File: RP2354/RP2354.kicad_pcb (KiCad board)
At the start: 2 copper layers, 37.4 x 23.2 mm, 38 parts, among them J1 USB_C_Receptacle_USB2.0_14P, J2 SWD, J3 Conn_01x12_Pin, J4 Conn_01x12_Pin, U1 TCR8BM33A_L3F, U14 RP2354A, Y1 Crystal

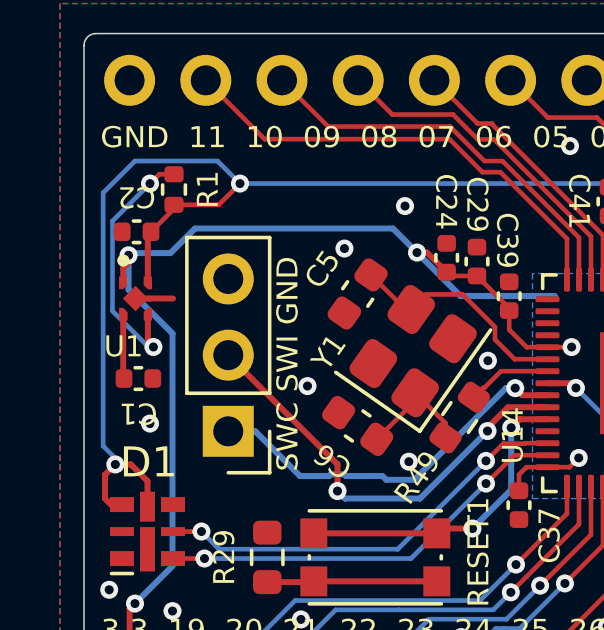
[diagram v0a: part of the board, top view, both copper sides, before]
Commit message: MPN's added for most parts. iBom export
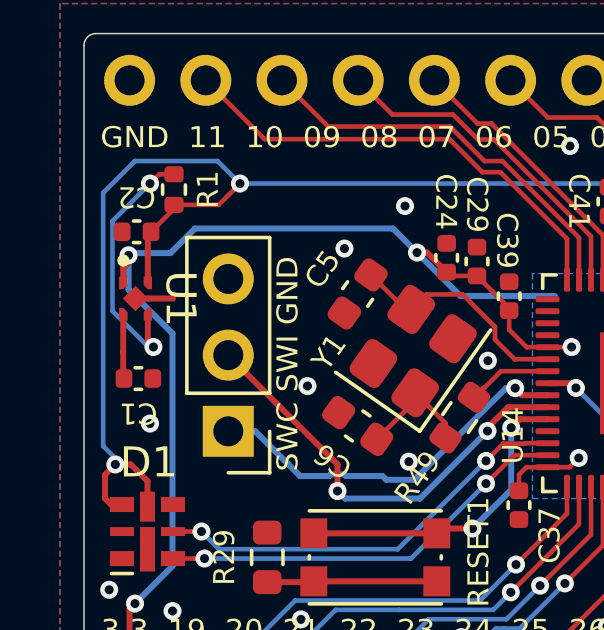
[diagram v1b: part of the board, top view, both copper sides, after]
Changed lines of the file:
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@@
 			)
 		)
+		(property "MFGR" "Adafruit (10-pack!)"
+			(at 0 0 0)
+			(unlocked yes)
+			(layer "F.Fab")
+			(hide yes)
+			(effects
+				(font
+					(size 1 1)
+					(thickness 0.15)
+				)
+			)
+		)
+		(property "MPN" "3341"
+			(at 0 0 0)
+			(unlocked yes)
+			(layer "F.Fab")
+			(hide yes)
+			(effects
+				(font
+					(size 1 1)
+					(thickness 0.15)
+				)
+			)
+		)
 		(property ki_fp_filters "LED*APA102*")
 		(sheetname "/")
@@
 		(tags "TCR8BM33A_L3F ")
 		(property "Reference" "U1"
-			(at 1.601769 0.399755 0)
+			(at 0 -1.5 270)
 			(unlocked yes)
 			(layer "F.SilkS")
 			(effects
 				(font
-					(size 0.7 0.7)
-					(thickness 0.1)
+					(size 1 1)
+					(thickness 0.15)
 				)
 			)
@@
 			)
 		)
+		(property "MFGR" "Toshiba Semiconductor and Storage"
+			(at 0 0 270)
+			(unlocked yes)
+			(layer "F.Fab")
+			(hide yes)
+			(effects
+				(font
+					(size 1 1)
+					(thickness 0.15)
+				)
+			)
+		)
+		(property "MPN" "TCR8BM33A,L3F"
+			(at 0 0 270)
+			(unlocked yes)
+			(layer "F.Fab")
+			(hide yes)
+			(effects
+				(font
+					(size 1 1)
+					(thickness 0.15)
+				)
+			)
+		)
 		(property ki_fp_filters "DFN5B_TOS")
 		(sheetname "/")
@@
 			(net 4 "+3V3")
 			(pinfunction "VOUT")
-			(pintype "output")
+			(pintype "power_out")
 		)
 		(pad "2" smd roundrect
@@
 			(net 58 "/VBIAS")
 			(pinfunction "VBIAS")
-			(pintype "power_in")
+			(pintype "input")
 		)
 		(pad "3" smd roundrect
@@
 			)
 		)
-		(property "MFGR" ""
+		(property "MFGR" "Samsung"
 			(at 0 0 55)
 			(unlocked yes)
@@
 			)
 		)
-		(property "MPN" ""
+		(property "MPN" "CL10C100JB8NFNC"
 			(at 0 0 55)
 			(unlocked yes)
@@
 			)
 		)
-		(property "MFGR" ""
+		(property "MFGR" "C&K"
 			(at 0 0 180)
 			(unlocked yes)
@@
 			)
 		)
-		(property "MPN" ""
+		(property "MPN" "KMR241G LFS"
 			(at 0 0 180)
 			(unlocked yes)
@@
 			)
 		)
-		(property "MFGR" "TDK"
+		(property "MFGR" "Samsung"
 			(at 0 0 145)
 			(unlocked yes)
@@
 			)
 		)
-		(property "MPN" "C1608C0G1H080D080AA"
+		(property "MPN" "CL10C100JB8NFNC"
 			(at 0 0 145)
 			(unlocked yes)
@@
 			(net 21 "unconnected-(U14-QSPI_SD3-Pad55)")
 			(pinfunction "QSPI_SD3")
-			(pintype "bidirectional")
+			(pintype "bidirectional+no_connect")
 		)
 		(pad "56" smd roundrect
@@
 			(net 18 "unconnected-(U14-QSPI_SCLK-Pad56)")
 			(pinfunction "QSPI_SCLK")
-			(pintype "output")
+			(pintype "output+no_connect")
 		)
 		(pad "57" smd roundrect
@@
 			(net 27 "unconnected-(U14-QSPI_SD0-Pad57)")
 			(pinfunction "QSPI_SD0")
-			(pintype "bidirectional")
+			(pintype "bidirectional+no_connect")
 		)
 		(pad "58" smd roundrect
@@
 			(net 26 "unconnected-(U14-QSPI_SD2-Pad58)")
 			(pinfunction "QSPI_SD2")
-			(pintype "bidirectional")
+			(pintype "bidirectional+no_connect")
 		)
 		(pad "59" smd roundrect
@@
 			(net 17 "unconnected-(U14-QSPI_SD1-Pad59)")
 			(pinfunction "QSPI_SD1")
-			(pintype "bidirectional")
+			(pintype "bidirectional+no_connect")
 		)
 		(pad "60" smd roundrect
@@
 			)
 		)
+		(property "MFGR" "C&K"
+			(at 0 0 0)
+			(unlocked yes)
+			(layer "F.Fab")
+			(hide yes)
+			(effects
+				(font
+					(size 1 1)
+					(thickness 0.15)
+				)
+			)
+		)
+		(property "MPN" "KMR241G LFS"
+			(at 0 0 0)
+			(unlocked yes)
+			(layer "F.Fab")
+			(hide yes)
+			(effects
+				(font
+					(size 1 1)
+					(thickness 0.15)
+				)
+			)
+		)
 		(sheetname "/")
 		(sheetfile "RP2354.kicad_sch")
@@
 					(thickness 0.15)
 				)
+			)
+		)
+		(property "MFGR" ""
+			(at 0 0 90)
+			(unlocked yes)
+			(layer "F.Fab")
+			(hide yes)
+			(effects
+				(font
+					(size 1 1)
+					(thickness 0.15)
+				)
+			)
+		)
+		(property "MPN" "TYPE-C-31-M-14"
+			(at 0 0 90)
+			(unlocked yes)
+			(layer "F.Fab")
+			(hide yes)
+			(effects
+				(font
+					(size 1 1)
+					(thickness 0.15)
+				)

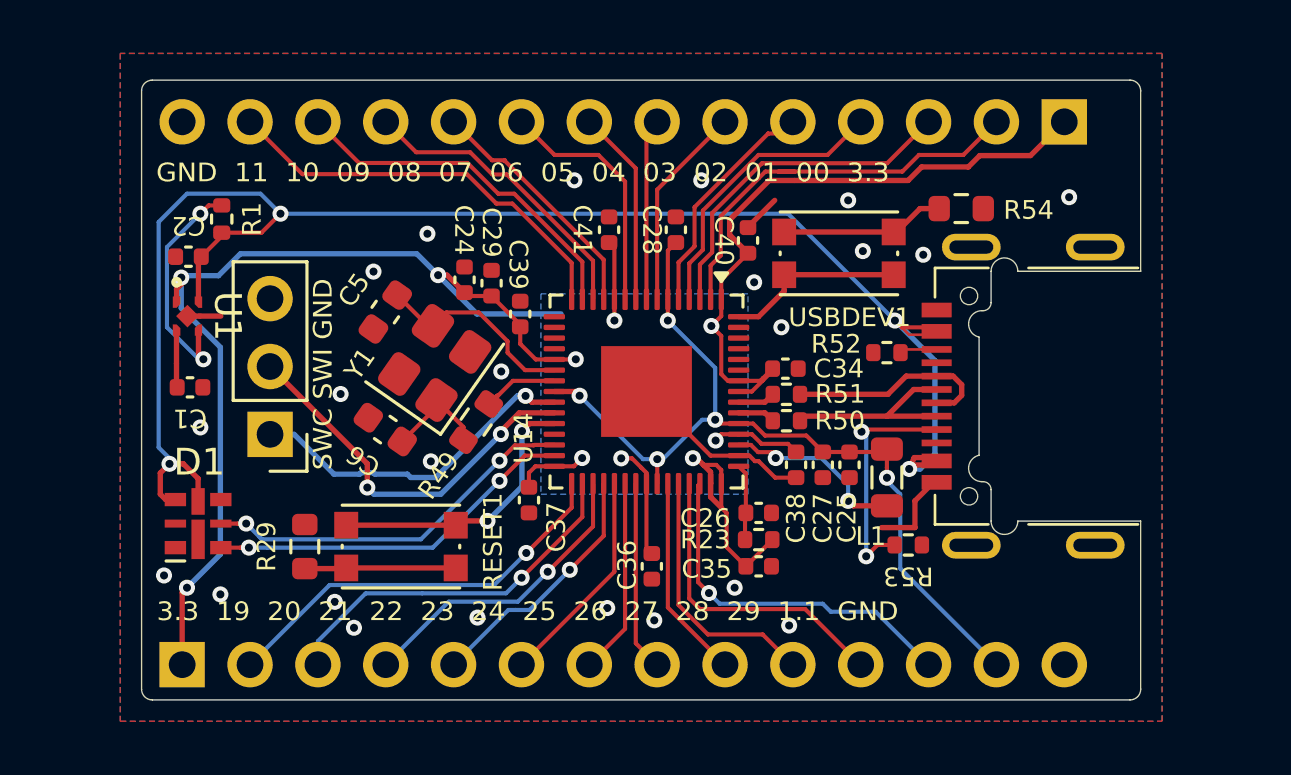
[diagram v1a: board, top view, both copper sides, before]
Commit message: Updated with a larger 3.3V regulator. The added pins break out +5V/USB and IO12 as well. The TCR8BM is just too fiddly for DIY boards and the datasheet isn't good enough.
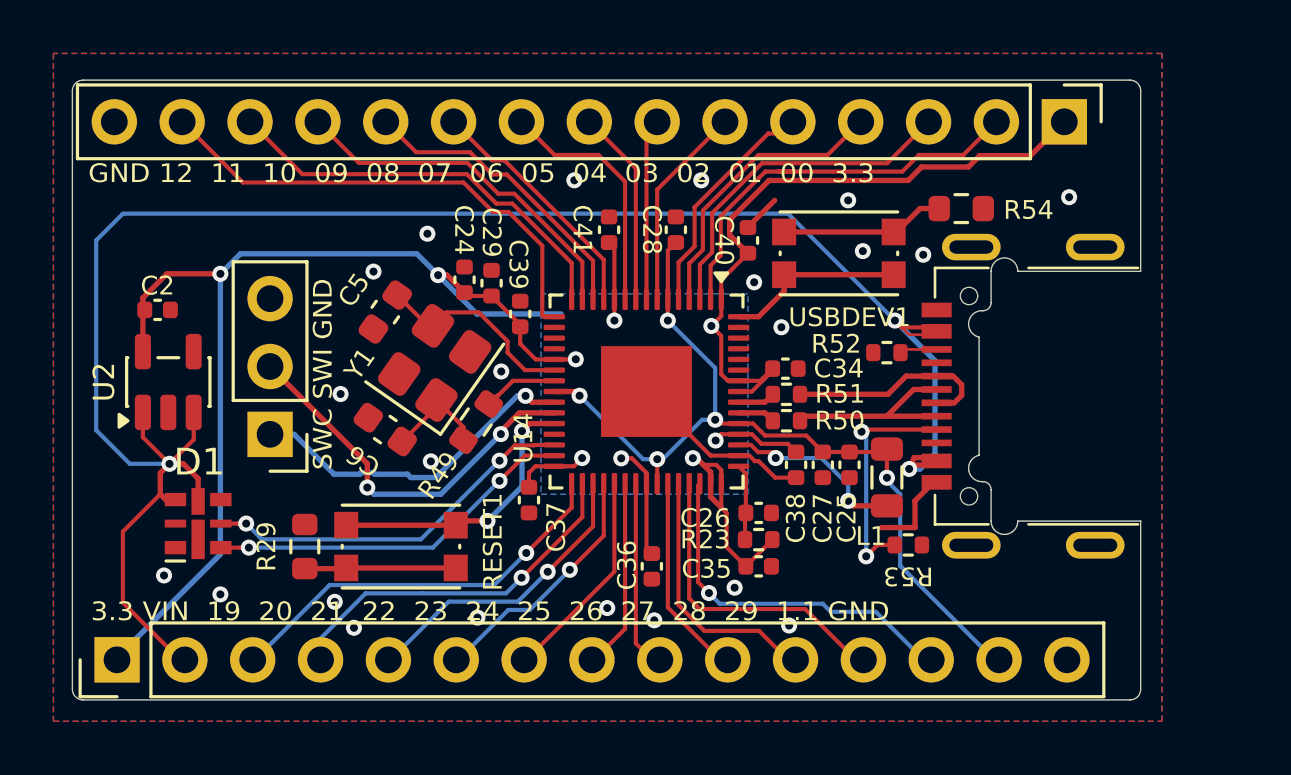
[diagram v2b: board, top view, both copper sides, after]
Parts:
- removed C1: 0.1uF, Capacitor_SMD:C_0402_1005Metric
- removed R1: 5.1k, Resistor_SMD:R_0402_1005Metric
- removed U1: TCR8BM33A_L3F, footprints:DFN5B_TOS
- added U2: AP2112K-3.3, Package_TO_SOT_SMD:SOT-23-5, F.Cu at (57.8, 45.3)
- J3, J4: value Conn_01x12_Pin -> Con; footprint Connector_PinHeader_2.54mm:PinHeader_1x14_P2.54mm_Vertical -> Connector_PinHeader_2.54mm:PinHeader_1x15_P2.54mm_Vertical
- moved J4 2.45 mm to (55.9, 55.7)
- moved C2 2.30 mm to (57.4, 42.6), turned to 180 degrees
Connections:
- C2 pad 2: /VIN -> +3V3
- D1 pad 1: /VIN -> /VBUS
- J1 pad A4: /VIN -> /VBUS
- J1 pad A9: /VIN -> /VBUS
- J1 pad B4: /VIN -> /VBUS
- J1 pad B9: /VIN -> /VBUS
- J3 pad 14: GND -> /o12
- J4 pad 10: /o27 -> /o26
- J4 pad 11: /o28 -> /o27
- J4 pad 12: /o29 -> /o28
- J4 pad 13: +1V1 -> /o29
- J4 pad 14: GND -> +1V1
- J4 pad 2: /o19 -> /VBUS
- J4 pad 3: /o20 -> /o19
- J4 pad 4: /o21 -> /o20
- J4 pad 5: /o22 -> /o21
- J4 pad 6: /o23 -> /o22
- J4 pad 7: /o24 -> /o23
- J4 pad 8: /o25 -> /o24
- J4 pad 9: /o26 -> /o25
- U14 pad 16: unconnected-(U14-GPIO12-Pad16) -> /o12
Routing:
- net /VBUS: track 0.00 -> 71.3 mm, vias 0 -> 3
- net /VIN: track 61.3 -> 0.00 mm, vias 4 -> 0
- net /o12: track 0.00 -> 18.5 mm
- net /CTRL: track 8.73 -> 0.00 mm, vias 2 -> 0
- net +3V3: track 86.2 -> 89.6 mm, vias 10 -> 9
- net /VBIAS: track 2.13 -> 0.00 mm
- net GND: track 12.5 -> 11.7 mm, vias 23 -> 22
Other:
- board size 37.4 x 23.2 mm -> 40 x 23.2 mm
- board text added: "3.3 VIN 19 20 21 22 23 24 25 26 27 28 29 1.1 GND"
- board text added: "GND 12 11 10 09 08 07 06 05 04 03 02 01 00 3.3"
- board text removed: "3.3 19 20 21 22 23 24 25 26 27 28 29 1.1 GND"
- board text removed: "GND 11 10 09 08 07 06 05 04 03 02 01 00 3.3"

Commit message: Layout tweak. Doc update.
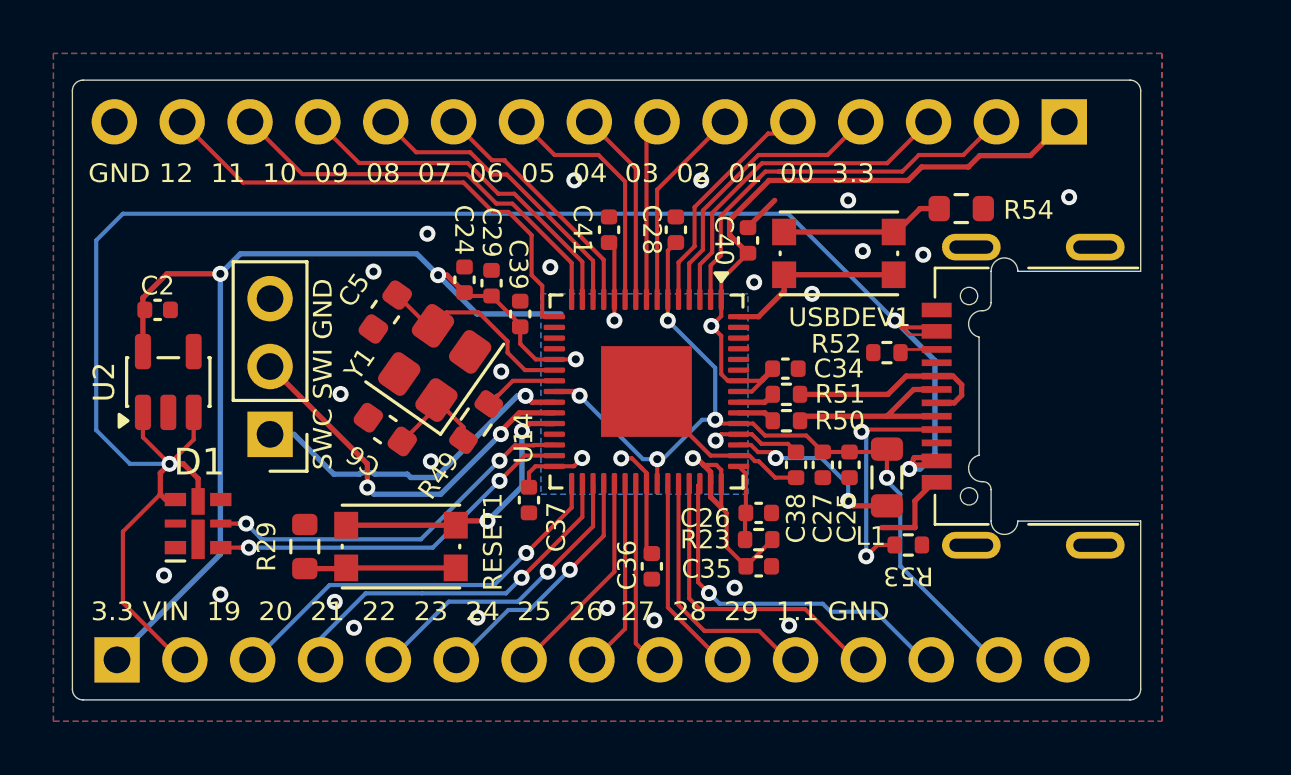
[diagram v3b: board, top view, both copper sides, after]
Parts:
- J3, J4: moved to B.Cu
- turned J3 to 90 degrees
- turned J4 to -90 degrees
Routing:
- net GND: vias 22 -> 23

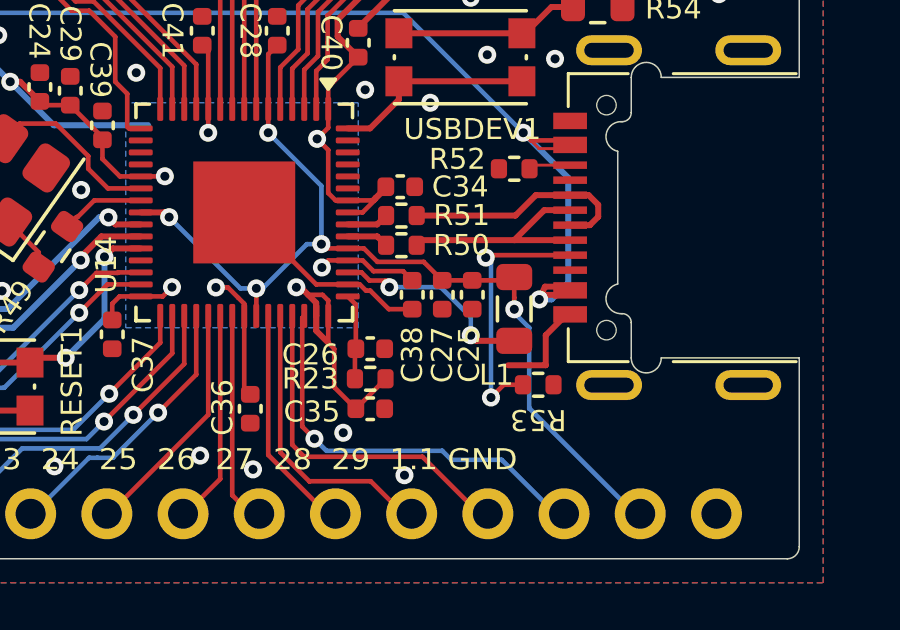
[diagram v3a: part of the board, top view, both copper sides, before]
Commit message: Swapped for larger inductor footprint on L1. 0805 resistor is correct.
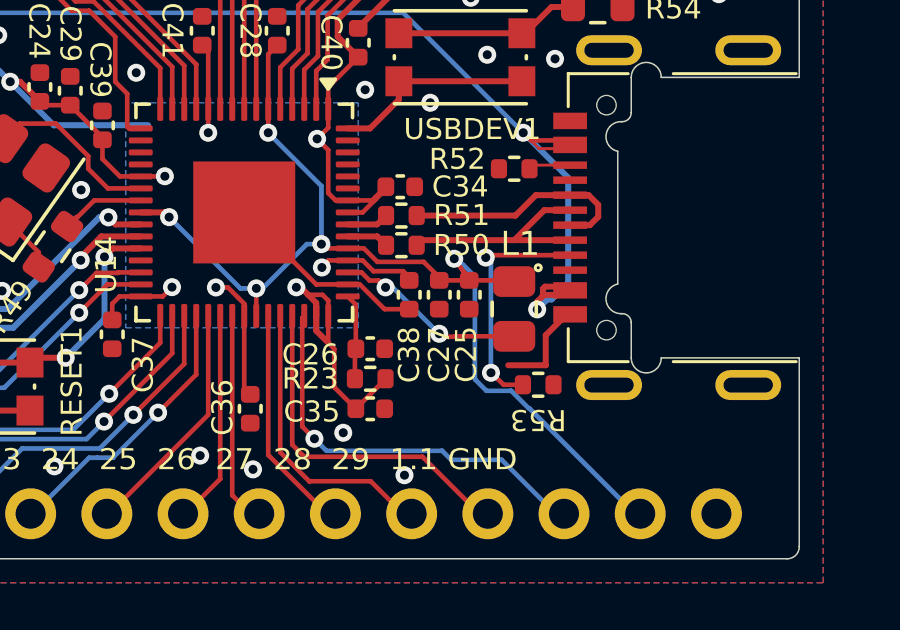
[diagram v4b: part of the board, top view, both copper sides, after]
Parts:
- L1: footprint Inductor_SMD:L_0805_2012Metric -> Resistor_SMD:R_0805_2012Metric
- moved C25 0.10 mm to (83.2, 48.4)
- moved C27 0.10 mm to (82.2, 48.4)
- moved C38 0.10 mm to (81.2, 48.4)
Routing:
- net +1V1: track 32.9 -> 35.8 mm
- net Net-(J1-CC1): track 8.82 -> 7.98 mm
